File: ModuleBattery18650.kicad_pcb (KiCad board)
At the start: 2 copper layers, 75 x 42 mm, 28 parts, among them J1 Connector_6p, T1 SI2323DS-T1-E3, T2 FDN337N, T3 SI2323DS-T1-E3, U1 MCP73832-2-OT, U2 MCP121T-315E

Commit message: adapted footprints
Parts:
- removed C2: 4.7uF, 0ESN_Lib:C_0805_2012Metric_Pad1.18x1.45mm_HandSolder
- removed D1: LED 2V, 0ESN_Lib:D_0603_1608Metric_Pad1.05x0.95mm_HandSolder
- removed JP2, JP3: Jumper_2_Bridged, 0ESN_Lib:PinHeader_1x02_P1.27mm_Vertical
- removed R4, R5: 1M, 0ESN_Lib:R_0603_1608Metric_Pad0.98x0.95mm_HandSolder
- removed R6: 0R NP, 0ESN_Lib:R_0603_1608Metric_Pad0.98x0.95mm_HandSolder
- removed U2: MCP121T-315E, Package_TO_SOT_SMD:SOT-23_Handsoldering
- added J2: Connector_2p_r, 0ESN_Lib:Connector_2p_m, F.Cu at (105.5, 56.2)
- added RS1: 0R NP, 0ESN_Lib:R_0603_1608Metric_Pad0.98x0.95mm_HandSolder, F.Cu at (111.7, 60.1)
- added RS2: 0R NP, 0ESN_Lib:R_0603_1608Metric_Pad0.98x0.95mm_HandSolder, F.Cu at (111.7, 62.6)
- added T4: SISH615ADN, 0ESN_Lib:PowerPAK 1212-8S, F.Cu at (116.8, 56.7)
- added T5: SISH615ADN, 0ESN_Lib:PowerPAK 1212-8S, F.Cu at (112.0, 56.7)
- added TP9: TestPoint, 0ESN_Lib:TestPoint_Pad_D1.0mm, F.Cu at (115.2, 60.1)
- J1: value Connector_6p -> Connector_2p; footprint 0ESN_Lib:Connector_6p_m -> 0ESN_Lib:Connector_2p_m
- R1: value 3k9 -> 1M
- R2: value 1k8 -> 1M
- R3: value 4k7 -> 1M
- T1: value SI2323DS-T1-E3 -> SISH615ADN; footprint Package_TO_SOT_SMD:SOT-23_Handsoldering -> 0ESN_Lib:PowerPAK 1212-8S
- T2: value FDN337N -> SISH615ADN; footprint Package_TO_SOT_SMD:SOT-23_Handsoldering -> 0ESN_Lib:PowerPAK 1212-8S
- T3: value SI2323DS-T1-E3 -> FDN337N
- U1: value MCP73832-2-OT -> MCP121T-315E; footprint 0ESN_Lib:SOT-23-5_HandSoldering -> Package_TO_SOT_SMD:SOT-23_Handsoldering
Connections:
- C1 pad 1: VDD -> Net-(C1-Pad1)
- F1 pad 2: /Vcharge -> Net-(C1-Pad1)
- J1 pad 2: /Vch -> GND
- JP1 pad 1: Net-(JP1-Pad1) -> /Vch
- R2 pad 1: Net-(JP2-Pad2) -> Net-(R2-Pad1)
- R2 pad 2: GND -> Net-(R2-Pad2)
- R3 pad 1: Net-(D1-Pad2) -> Net-(R2-Pad1)
- R3 pad 2: VDD -> Net-(R3-Pad2)
- T1 pad 2: Net-(R4-Pad1) -> Net-(C1-Pad1)
- T1 pad 3: /Vcharge -> Net-(JP1-Pad2)
- T2 pad 1: Net-(R4-Pad2) -> Net-(JP1-Pad2)
- T2 pad 2: GND -> Net-(C1-Pad1)
- T2 pad 3: Net-(R5-Pad2) -> Net-(R2-Pad1)
- T3 pad 1: Net-(R5-Pad2) -> Net-(R2-Pad2)
- T3 pad 2: Net-(R4-Pad1) -> GND
- T3 pad 3: Vbat -> Net-(R3-Pad2)
- TP2 pad 1: /Vcharge -> GND
- TP3 pad 1: VDD -> Net-(JP1-Pad2)
- TP4 pad 1: GND -> Net-(C1-Pad1)
- TP5 pad 1: Net-(R4-Pad1) -> Net-(R2-Pad1)
- TP6 pad 1: Net-(R4-Pad2) -> Net-(R2-Pad2)
- TP7 pad 1: Net-(R5-Pad2) -> Net-(R3-Pad2)
- TP8 pad 1: Vbat -> Net-(RS2-Pad2)
- U1 pad 1: Net-(D1-Pad1) -> Net-(R2-Pad2)
- U1 pad 2: GND -> Net-(R2-Pad1)
- U1 pad 3: /Vcharge -> GND
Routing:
- net VDD: track 59.9 -> 0.00 mm, vias 7 -> 0
- net Net-(R3-Pad2): track 0.00 -> 59.9 mm, vias 0 -> 1
- net /Vcharge: track 47.0 -> 0.00 mm, vias 5 -> 0
- net Net-(JP1-Pad2): track 1.63 -> 42.9 mm, vias 0 -> 8
- net Net-(C1-Pad1): track 0.00 -> 33.7 mm
- net Net-(R4-Pad1): track 28.0 -> 0.00 mm, vias 2 -> 0
- net Vbat: track 26.0 -> 0.00 mm
- net Net-(RS2-Pad2): track 0.00 -> 14.7 mm
- net Net-(R2-Pad2): track 0.00 -> 10.1 mm
- net /Vch: track 23.3 -> 13.9 mm
- net Net-(R4-Pad2): track 8.08 -> 0.00 mm
- net Net-(JP1-Pad1): track 7.69 -> 0.00 mm
- net Net-(R5-Pad2): track 7.45 -> 0.00 mm
- net Net-(R2-Pad1): track 0.00 -> 3.35 mm
- net Net-(D1-Pad1): track 2.02 -> 0.00 mm
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- added copper zone on B.Cu, net Net-(C1-Pad1)
- added copper zone on F.Cu, net Net-(C1-Pad1)
- added copper zone on B.Cu, net Net-(JP1-Pad2)
- removed copper zone on B.Cu, net /Vcharge
- removed copper zone on F.Cu, net /Vcharge
- removed copper zone on B.Cu, net VDD
- removed copper zone on F.Cu, net VDD

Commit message: added output files
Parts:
- moved J2 24.5 mm to (85.2, 69.8), turned to 90 degrees
- moved TP9 15.1 mm to (128.4, 67.3)
- moved RS2 13.3 mm to (124.2, 67.3)
- moved T5 12.7 mm to (105.0, 67.3)
- moved T4 12.3 mm to (110.6, 67.3)
- moved RS1 9.71 mm to (118.2, 67.3)
- moved J1 6.50 mm to (90.3, 69.8)
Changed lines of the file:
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@@
   (net 10 "Net-(RS2-Pad2)")
   (footprint "0ESN_Lib:R_0603_1608Metric_Pad0.98x0.95mm_HandSolder" (layer "F.Cu")
-    (at 111.725 62.605)
+    (at 124.2125 67.31)
     (descr "Resistor SMD 0603 (1608 Metric), square (rectangular) end terminal, IPC_7351 nominal with elongated pad for handsoldering. (Body size source: IPC-SM-782 page 72, https://www.pcb-3d.com/wordpress/wp-content/uploads/ipc-sm-782a_amendment_1_and_2.pdf), generated with kicad-footprint-generator")
     (tags "resistor handsolder")
@@
   )
   (footprint "0ESN_Lib:Connector_2p_m" (layer "F.Cu")
-    (at 88.875 76.2 90)
+    (at 90.28 69.85 90)
     (descr "Through hole straight pin header, 1x06, 2.54mm pitch, single row")
     (tags "Through hole pin header THT 1x06 2.54mm single row")
@@
   )
   (footprint "0ESN_Lib:R_0603_1608Metric_Pad0.98x0.95mm_HandSolder" (layer "F.Cu")
-    (at 111.725 60.095)
+    (at 118.22 67.31)
     (descr "Resistor SMD 0603 (1608 Metric), square (rectangular) end terminal, IPC_7351 nominal with elongated pad for handsoldering. (Body size source: IPC-SM-782 page 72, https://www.pcb-3d.com/wordpress/wp-content/uploads/ipc-sm-782a_amendment_1_and_2.pdf), generated with kicad-footprint-generator")
     (tags "resistor handsolder")
@@
   )
   (footprint "0ESN_Lib:Connector_2p_m" (layer "F.Cu")
-    (at 105.5 56.17)
+    (at 85.2 69.85 90)
     (descr "Through hole straight pin header, 1x06, 2.54mm pitch, single row")
     (tags "Through hole pin header THT 1x06 2.54mm single row")
@@
     (property "Sheetname" "")
     (attr through_hole)
-    (fp_text reference "J2" (at 0 -2.3) (layer "F.SilkS")
-      (effects (font (size 1 1) (thickness 0.15)))
-    )
-    (fp_text value "Connector_2p_r" (at -0.05 4.84) (layer "F.Fab")
-      (effects (font (size 1 1) (thickness 0.15)))
-    )
-    (fp_text user "1" (at 4 0 unlocked) (layer "F.SilkS")
-      (effects (font (size 1 1) (thickness 0.15)))
-    )
-    (fp_text user "${REFERENCE}" (at 0 6.35 90) (layer "F.Fab")
+    (fp_text reference "J2" (at 0 -2.3 90) (layer "F.SilkS")
+      (effects (font (size 1 1) (thickness 0.15)))
+    )
+    (fp_text value "Connector_2p_r" (at -0.05 4.84 90) (layer "F.Fab")
+      (effects (font (size 1 1) (thickness 0.15)))
+    )
+    (fp_text user "1" (at 4 0 90 unlocked) (layer "F.SilkS")
+      (effects (font (size 1 1) (thickness 0.15)))
+    )
+    (fp_text user "${REFERENCE}" (at 0 6.35) (layer "F.Fab")
       (effects (font (size 1 1) (thickness 0.15)))
     )
@@
     (fp_line (start 3.5 4.09) (end -3.5 4.09) (layer "F.Fab") (width 0.1))
     (fp_line (start 3.5 -1.5) (end 3.5 4.09) (layer "F.Fab") (width 0.1))
-    (pad "1" thru_hole rect (at 0 0) (size 1.7 1.7) (drill 1) (layers *.Cu *.Mask)
+    (pad "1" thru_hole rect (at 0 0 90) (size 1.7 1.7) (drill 1) (layers *.Cu *.Mask)
       (net 6 "/Vbat") (pinfunction "P1") (pintype "passive"))
-    (pad "2" thru_hole oval (at 0 2.54) (size 1.7 1.7) (drill 1) (layers *.Cu *.Mask)
+    (pad "2" thru_hole oval (at 0 2.54 90) (size 1.7 1.7) (drill 1) (layers *.Cu *.Mask)
       (net 2 "GND") (pinfunction "P2") (pintype "passive"))
     (model "C:/Workspace/03_CAD_Output/imports/022232061.stp"
@@
   )
   (footprint "0ESN_Lib:PowerPAK 1212-8S" (layer "F.Cu")
-    (at 111.98 56.68)
+    (at 104.9625 67.31)
     (property "Sheetfile" "ModuleBattery18650.kicad_sch")
     (property "Sheetname" "")
@@
   )
   (footprint "0ESN_Lib:TestPoint_Pad_D1.0mm" (layer "F.Cu")
-    (at 115.16 60.1)
+    (at 128.38 67.31)
     (descr "SMD pad as test Point, diameter 1.0mm")
     (tags "test point SMD pad")
@@
   )
   (footprint "0ESN_Lib:PowerPAK 1212-8S" (layer "F.Cu")
-    (at 116.84 56.68)
-    (property "Sheetfile" "ModuleBattery18650.kicad_sch")
-    (property "Sheetname" "")
+    (at 110.6 67.31)
+    (property "Sheetfile" "ModuleBattery18650.kicad_sch")
+    (property "Sheetname" "")

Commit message: progress for the pcb
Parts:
- C1: moved to B.Cu
- moved JP1 104.7 mm to (36.9, 82.5)
- moved R1 81.6 mm to (77.3, 31.8)
- moved C1 81.0 mm to (75.0, 34.3), turned to 0 degrees
- moved T1 80.5 mm to (44.6, 85.1), turned to 90 degrees
- moved R2 75.1 mm to (82.7, 33.0)
- moved U1 69.3 mm to (82.7, 36.8), turned to -90 degrees
- moved R3 63.1 mm to (91.5, 33.0), turned to 180 degrees
- moved BT1 63.0 mm to (106.9, 34.3)
- moved F1 63.0 mm to (70.0, 34.3)
- moved TP5 61.7 mm to (81.6, 31.2), turned to 0 degrees
- moved TP8 61.1 mm to (82.7, 28.4), turned to 0 degrees
- moved T2 60.7 mm to (77.3, 34.3), turned to 0 degrees
- moved J1 59.0 mm to (34.1, 87.9), turned to 0 degrees
- moved TP1 58.9 mm to (158.8, 52.1), turned to 0 degrees
- moved TP6 55.4 mm to (85.2, 39.6), turned to 0 degrees
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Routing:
- net GND: track 132.7 -> 45.3 mm, vias 15 -> 0
- net Net-(R3-Pad2): track 59.9 -> 12.4 mm, vias 1 -> 0
- net Net-(JP1-Pad2): track 42.9 -> 7.51 mm, vias 8 -> 0
- net Net-(C1-Pad1): track 33.7 -> 19.1 mm, vias 0 -> 1
- net /Vch: track 13.9 -> 0.00 mm
- net Net-(R2-Pad1): track 3.35 -> 17.0 mm
- net Net-(RS2-Pad2): track 14.7 -> 14.0 mm
- net Net-(R2-Pad2): track 10.1 -> 9.53 mm
- removed copper zone on B.Cu, net /Vch
- removed copper zone on B.Cu, net GND
- removed copper zone on F.Cu, net GND
- removed copper zone on B.Cu, net Net-(BT1-Pad1)
- removed copper zone on B.Cu, net Net-(C1-Pad1)
- removed copper zone on F.Cu, net Net-(C1-Pad1)
- removed copper zone on B.Cu, net Net-(JP1-Pad2)
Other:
- board outline removed

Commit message: progress on pcb
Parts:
- BT1: moved to B.Cu
- C1, F1: moved to F.Cu
- moved T5 119.3 mm to (161.5, 114.0), turned to 180 degrees
- moved TP8 112.4 mm to (158.4, 111.4)
- moved T2 106.5 mm to (143.5, 117.8)
- moved F1 106.2 mm to (135.6, 117.8)
- moved R2 106.2 mm to (148.3, 116.5)
- moved R3 106.2 mm to (157.2, 116.5)
- moved T3 106.2 mm to (153.3, 120.3)
- moved TP6 106.2 mm to (150.8, 123.1)
- moved TP7 106.2 mm to (156.2, 118.4)
- moved R1 106.2 mm to (142.9, 115.2)
- moved RS1 106.2 mm to (142.9, 120.3)
- moved RS2 106.2 mm to (156.1, 113.7)
- moved TP4 106.2 mm to (141.9, 122.2)
- moved TP5 106.2 mm to (147.2, 114.7)
- moved U1 106.2 mm to (148.3, 120.3)
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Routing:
- net GND: track 45.3 -> 129.0 mm, vias 0 -> 7
- net Net-(JP1-Pad2): track 7.51 -> 30.1 mm
- net Net-(R2-Pad1): track 17.0 -> 32.4 mm, vias 0 -> 2
- net /Vbat: track 0.00 -> 14.6 mm
- net /Vch: track 0.00 -> 7.62 mm
- net Net-(BT1-Pad1): track 17.3 -> 20.7 mm
- net Net-(RS2-Pad2): track 14.0 -> 14.9 mm
- net Net-(C1-Pad1): track 19.1 -> 19.9 mm, vias 1 -> 0
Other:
- board outline added: 100 x 30 mm

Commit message: rev00
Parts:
- added D1: LED, 0ESN_Lib:D_0603_1608Metric_Pad1.05x0.95mm_HandSolder, B.Cu at (127.0, 101.6)
- added R4: 150R, Resistor_SMD:R_0805_2012Metric_Pad1.20x1.40mm_HandSolder, B.Cu at (125.1, 101.6)
- added REF**: MountingHole_4.3mm_M4, MountingHole:MountingHole_4.3mm_M4, F.Cu at (114.0, 101.0)
- added REF**: MountingHole_4.3mm_M4, MountingHole:MountingHole_4.3mm_M4, F.Cu at (187.0, 101.0)
- added REF**: MountingHole_4.3mm_M4, MountingHole:MountingHole_4.3mm_M4, F.Cu at (149.0, 101.0)
- J1, J2: moved to B.Cu
- JP1: footprint 0ESN_Lib:PinHeader_1x02_P1.27mm_Vertical -> Jumper:SolderJumper-2_P1.3mm_Open_RoundedPad1.0x1.5mm
- R1, R2, R3, RS1, RS2: footprint 0ESN_Lib:R_0603_1608Metric_Pad0.98x0.95mm_HandSolder -> Resistor_SMD:R_0603_1608Metric_Pad0.98x0.95mm_HandSolder
- moved J2 13.7 mm to (160.8, 100.3), turned to 180 degrees
- moved J1 12.0 mm to (137.2, 102.9)
- moved TP3 9.52 mm to (130.0, 108.2)
- moved TP1 3.62 mm to (133.3, 102.9)
- moved JP1 2.23 mm to (130.8, 104.8), turned to -90 degrees
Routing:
- net GND: track 129.0 -> 147.4 mm
- net Net-(JP1-Pad2): track 30.1 -> 40.2 mm, vias 0 -> 1
- net /Vbat: track 14.6 -> 17.0 mm
- net Net-(D1-Pad2): track 0.00 -> 1.96 mm
- added copper zone on B.Cu, net GND
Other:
- board size 100 x 30 mm -> 83 x 30 mm
- board text added: "CHARGE"
- board text added: "ModuleBattery18650 Nicolas Esseiva 2023.04.08 - r00"
- board text added: "POWER"

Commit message: revision 01
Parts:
- C1: footprint 0ESN_Lib:C_0805_2012Metric_Pad1.18x1.45mm_HandSolder -> Capacitor_SMD:C_0805_2012Metric_Pad1.18x1.45mm_HandSolder
- D1: footprint 0ESN_Lib:D_0603_1608Metric_Pad1.05x0.95mm_HandSolder -> Diode_SMD:D_0603_1608Metric_Pad1.05x0.95mm_HandSolder
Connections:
- D1 pad 1: Net-(JP1-Pad2) -> Net-(D1-Pad1)
- JP1 pad 2: Net-(JP1-Pad2) -> Net-(D1-Pad1)
- R1 pad 1: Net-(JP1-Pad2) -> Net-(D1-Pad1)
- T1 pad 1: GND -> Net-(C1-Pad1)
- T1 pad 3: Net-(JP1-Pad2) -> Net-(C1-Pad1)
- T2 pad 1: Net-(JP1-Pad2) -> Net-(C1-Pad1)
- T2 pad 3: Net-(R2-Pad1) -> Net-(C1-Pad1)
- T4 pad 1: Net-(R3-Pad2) -> Net-(R2-Pad1)
- T4 pad 3: Net-(RS2-Pad2) -> Net-(R2-Pad1)
- T5 pad 1: GND -> /Vbat
- T5 pad 3: Net-(RS2-Pad2) -> /Vbat
- TP3 pad 1: Net-(JP1-Pad2) -> Net-(D1-Pad1)
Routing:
- net Net-(JP1-Pad2): track 40.2 -> 0.00 mm, vias 1 -> 0
- net Net-(D1-Pad1): track 0.00 -> 39.5 mm, vias 0 -> 3
- net Net-(C1-Pad1): track 19.9 -> 32.4 mm
- net GND: track 147.4 -> 136.5 mm
- net /Vbat: track 17.0 -> 24.3 mm
- net Net-(R2-Pad1): track 32.4 -> 34.1 mm, vias 2 -> 3
- net Net-(R3-Pad2): track 12.4 -> 11.8 mm
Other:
- board text added: "ModuleBattery18650 Nicolas Esseiva 2023.05.18 - r01"
- board text removed: "ModuleBattery18650 Nicolas Esseiva 2023.04.08 - r00"

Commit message: ^small changes
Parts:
- H1, H2, H3: renamed from REF**; value MountingHole_4.3mm_M4 -> MountingHole
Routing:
- net Net-(RS2-Pad2): track 14.9 -> 28.8 mm
- net Net-(R2-Pad1): track 34.1 -> 29.5 mm, vias 3 -> 2
- net Net-(R3-Pad2): track 11.8 -> 13.2 mm, vias 0 -> 2

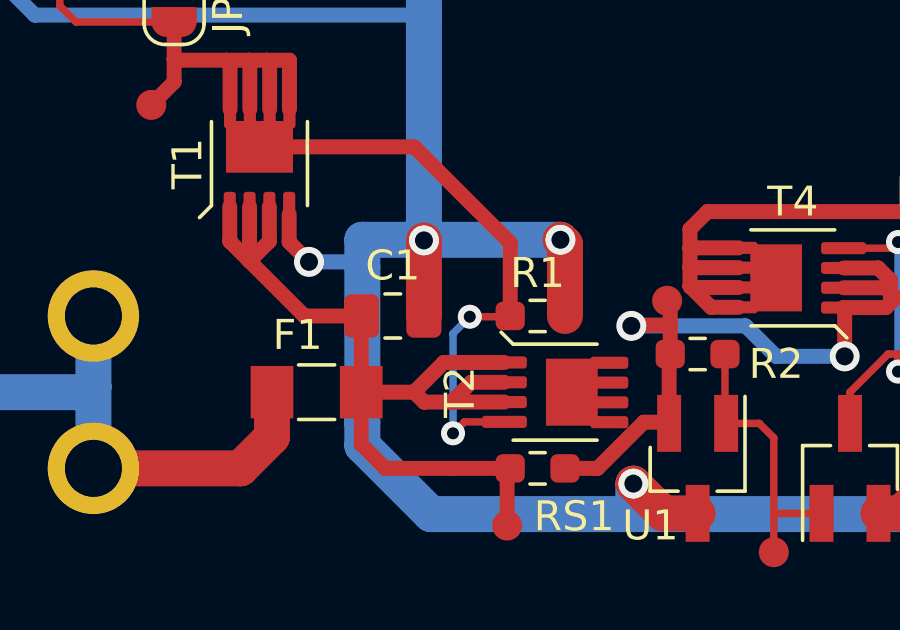
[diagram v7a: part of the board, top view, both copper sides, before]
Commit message: Update ModuleBattery18650.kicad_pcb
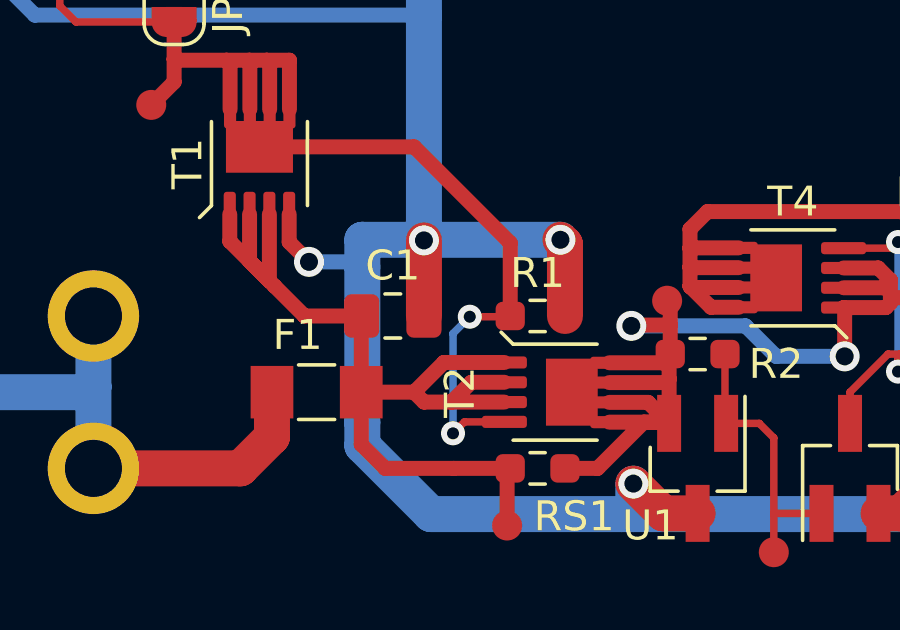
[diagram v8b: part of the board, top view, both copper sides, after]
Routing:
- net Net-(R2-Pad1): track 29.5 -> 38.0 mm
- net Net-(C1-Pad1): track 32.4 -> 32.9 mm
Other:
- board text added: "ModuleBattery18650 Nicolas Esseiva 2023.06.21 - r01"
- board text added: "TODO: 1. Vérifier l'espacement pour le porte batterie !!! Actuellement, le max n'est pas assez... 2. Vérifier si les connecteurs sont OK sur le montage actuel"
- board text removed: "ModuleBattery18650 Nicolas Esseiva 2023.05.18 - r01"
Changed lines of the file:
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@@
     (effects (font (size 1 1) (thickness 0.15)) (justify mirror))
   )
-  (gr_text "ModuleBattery18650\nNicolas Esseiva\n2023.05.18 - r01" (at 125.73 107.95 180) (layer "B.SilkS")
+  (gr_text "ModuleBattery18650\nNicolas Esseiva\n2023.06.21 - r01" (at 125.73 107.95 180) (layer "B.SilkS")
     (effects (font (size 1.27 1.27) (thickness 0.3)) (justify mirror))
   )
   (gr_text "CHARGE" (at 132.715 100.965 270) (layer "B.SilkS")
     (effects (font (size 1 1) (thickness 0.15)) (justify mirror))
+  )
+  (gr_text "TODO:\n1. Vérifier l'espacement pour le porte batterie !!!\n   Actuellement, le max n'est pas assez...\n2. Vérifier si les connecteurs sont OK sur le montage actuel" (at 148.336 88.392) (layer "User.1")
+    (effects (font (size 1.5 1.5) (thickness 0.3)))
   )
   (segment (start 134.0725 119.2675) (end 134.0725 117.78) (width 1.2) (layer "F.Cu") (net 1))
@@
   (segment (start 137.0625 115.24) (end 135.154 115.24) (width 0.5) (layer "F.Cu") (net 3))
   (segment (start 139.8012 116.79) (end 138.8112 117.78) (width 0.5) (layer "F.Cu") (net 3))
-  (segment (start 132.665 111.595) (end 132.665 112.751) (width 0.5) (layer "F.Cu") (net 3))
-  (segment (start 133.985 112.751) (end 133.325 113.411) (width 0.5) (layer "F.Cu") (net 3))
-  (segment (start 133.325 111.595) (end 133.325 113.411) (width 0.5) (layer "F.Cu") (net 3))
+  (segment (start 133.325 111.85) (end 133.325 113.411) (width 0.5) (layer "F.Cu") (net 3))
+  (segment (start 133.985 111.85) (end 133.985 114.071) (width 0.5) (layer "F.Cu") (net 3))
+  (segment (start 133.985 114.071) (end 134.163 114.249) (width 0.5) (layer "F.Cu") (net 3))
   (segment (start 138.8112 117.78) (end 137.0475 117.78) (width 0.5) (layer "F.Cu") (net 3))
   (segment (start 141.91 120.4235) (end 142.0135 120.32) (width 0.5) (layer "F.Cu") (net 3))
   (segment (start 140.7156 117.45) (end 140.0556 118.11) (width 0.5) (layer "F.Cu") (net 3))
   (segment (start 141.82 117.45) (end 140.7156 117.45) (width 0.5) (layer "F.Cu") (net 3))
-  (segment (start 133.985 111.595) (end 133.985 112.751) (width 0.5) (layer "F.Cu") (net 3))
-  (segment (start 132.665 112.751) (end 133.325 113.411) (width 0.5) (layer "F.Cu") (net 3))
+  (segment (start 132.665 112.751) (end 133.985 114.071) (width 0.5) (layer "F.Cu") (net 3))
   (segment (start 141.82 116.79) (end 139.8012 116.79) (width 0.5) (layer "F.Cu") (net 3))
   (segment (start 141.82 118.11) (end 140.0556 118.11) (width 0.5) (layer "F.Cu") (net 3))
@@
   (segment (start 137.0475 117.78) (end 137.0475 119.5215) (width 0.5) (layer "F.Cu") (net 3))
   (segment (start 139.1412 118.11) (end 138.8112 117.78) (width 0.5) (layer "F.Cu") (net 3))
+  (segment (start 135.154 115.24) (end 134.163 114.249) (width 0.5) (layer "F.Cu") (net 3))
   (segment (start 137.0475 117.78) (end 137.0475 115.255) (width 0.5) (layer "F.Cu") (net 3))
-  (segment (start 135.154 115.24) (end 133.325 113.411) (width 0.5) (layer "F.Cu") (net 3))
+  (segment (start 133.325 113.411) (end 133.985 114.071) (width 0.5) (layer "F.Cu") (net 3))
+  (segment (start 132.665 111.85) (end 132.665 112.751) (width 0.5) (layer "F.Cu") (net 3))
   (segment (start 133.35 102.87) (end 137.16 102.87) (width 0.5) (layer "F.Cu") (net 4))
   (segment (start 130.81 104.14) (end 130.81 103.378) (width 0.5) (layer "F.Cu") (net 4))
@@
   (segment (start 149.63 114.95) (end 148.706508 114.95) (width 0.5) (layer "F.Cu") (net 9))
   (segment (start 149.63 112.97) (end 148.015 112.97) (width 0.5) (layer "F.Cu") (net 9))
+  (segment (start 147.27 118.78) (end 147.31 118.82) (width 0.5) (layer "F.Cu") (net 10))
   (segment (start 144.926 120.32) (end 146.466 118.78) (width 0.5) (layer "F.Cu") (net 10))
+  (segment (start 145.315 116.8) (end 147.0575 116.8) (width 0.5) (layer "F.Cu") (net 10))
   (segment (start 158.0625 115.1365) (end 158.0625 116.51) (width 0.5) (layer "F.Cu") (net 10))
   (segment (start 153.125 114.96) (end 154.534 114.96) (width 0.5) (layer "F.Cu") (net 10))
@@
   (segment (start 153.162 114.997) (end 153.125 114.96) (width 0.5) (layer "F.Cu") (net 10))
   (segment (start 156.134 114.6285) (end 157.5545 114.6285) (width 0.5) (layer "F.Cu") (net 10))
+  (segment (start 145.315 117.46) (end 147.188 117.46) (width 0.5) (layer "F.Cu") (net 10))
   (segment (start 157.5545 114.6285) (end 158.0625 115.1365) (width 0.5) (layer "F.Cu") (net 10))
+  (segment (start 145.315 118.78) (end 147.27 118.78) (width 0.5) (layer "F.Cu") (net 10))
   (segment (start 153.125 113.64) (end 154.28 113.64) (width 0.5) (layer "F.Cu") (net 10))
   (segment (start 154.686 114.554) (end 154.686 114.808) (width 0.5) (layer "F.Cu") (net 10))
@@
   (segment (start 153.125 114.3) (end 154.432 114.3) (width 0.5) (layer "F.Cu") (net 10))
   (segment (start 147.3475 116.51) (end 147.3475 115.5425) (width 0.5) (layer "F.Cu") (net 10))
-  (segment (start 147.31 118.82) (end 147.31 116.5475) (width 0.5) (layer "F.Cu") (net 10))
   (segment (start 147.31 116.5475) (end 147.3475 116.51) (width 0.5) (layer "F.Cu") (net 10))
   (segment (start 154.432 114.3) (end 154.686 114.046) (width 0.5) (layer "F.Cu") (net 10))
+  (segment (start 145.315 118.12) (end 146.61 118.12) (width 0.5) (layer "F.Cu") (net 10))
+  (segment (start 147.188 117.46) (end 147.31 117.338) (width 0.5) (layer "F.Cu") (net 10))
   (segment (start 154.28 113.64) (end 154.686 114.046) (width 0.5) (layer "F.Cu") (net 10))
   (segment (start 156.134 114.6285) (end 154.7605 114.6285) (width 0.5) (layer "F.Cu") (net 10))
+  (segment (start 147.31 117.338) (end 147.31 116.5475) (width 0.5) (layer "F.Cu") (net 10))
+  (segment (start 147.0575 116.8) (end 147.3475 116.51) (width 0.5) (layer "F.Cu") (net 10))
   (segment (start 147.3475 115.5425) (end 147.3475 114.8355) (width 0.5) (layer "F.Cu") (net 10))
   (segment (start 146.0775 115.5425) (end 146.05 115.57) (width 0.5) (layer "F.Cu") (net 10))
   (segment (start 154.7605 114.6285) (end 154.686 114.554) (width 0.5) (layer "F.Cu") (net 10))
-  (segment (start 147.27 118.78) (end 147.31 118.82) (width 0.5) (layer "F.Cu") (net 10))
+  (segment (start 146.61 118.12) (end 147.31 118.82) (width 0.5) (layer "F.Cu") (net 10))
+  (segment (start 147.31 118.82) (end 147.31 117.338) (width 0.5) (layer "F.Cu") (net 10))
   (segment (start 153.162 116.586) (end 153.162 114.997) (width 0.5) (layer "F.Cu") (net 10))
   (segment (start 154.686 114.046) (end 154.686 114.554) (width 0.5) (layer "F.Cu") (net 10))
@@
     (connect_pads (clearance 0.17))
     (min_thickness 0.254) (filled_areas_thickness no)
-    (fill (thermal_gap 0.508) (thermal_bridge_width 0.508))
+    (fill yes (thermal_gap 0.508) (thermal_bridge_width 0.508))
     (polygon
       (pts
